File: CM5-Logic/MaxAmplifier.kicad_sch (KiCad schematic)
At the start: 8 parts, among them U12 MAX98357AETE_T, U13 MAX98357AETE_T

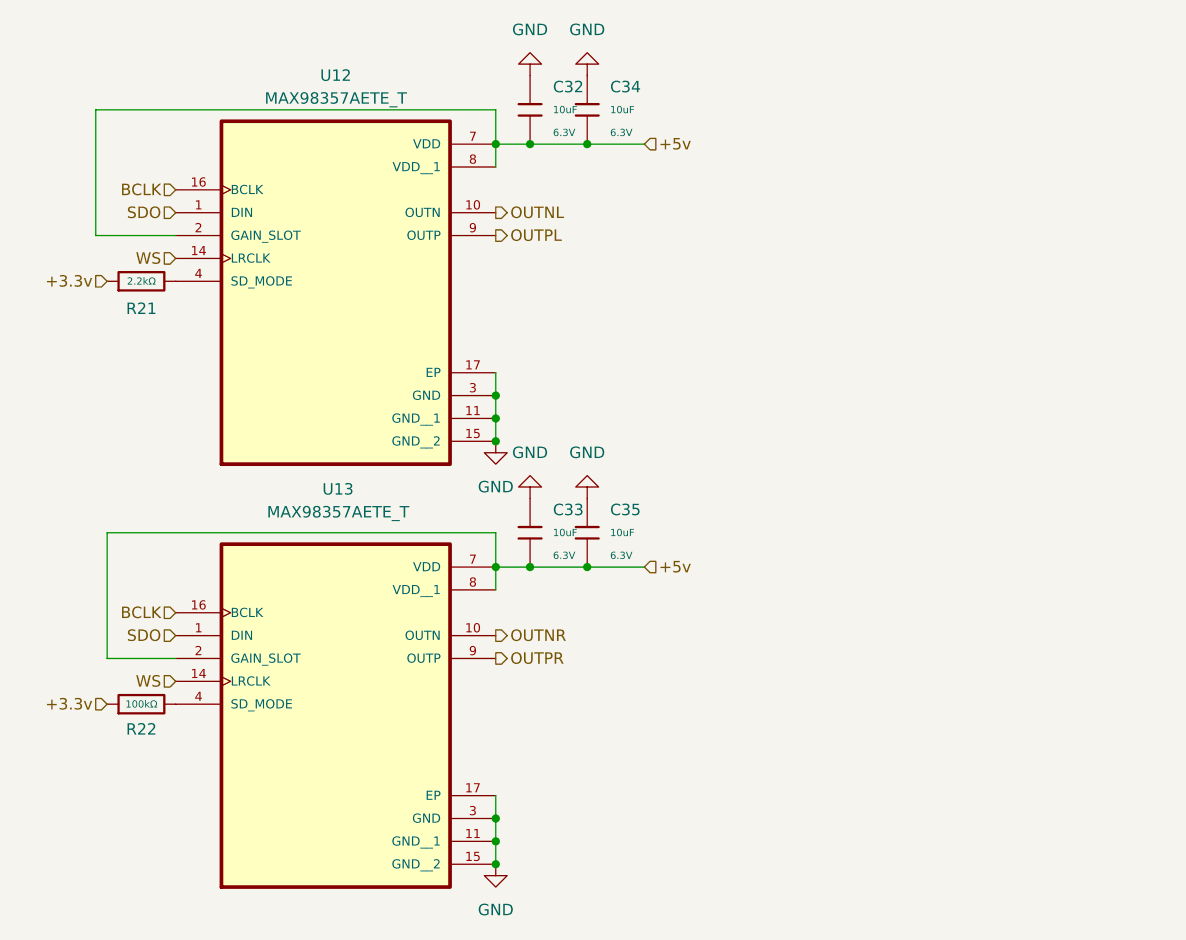
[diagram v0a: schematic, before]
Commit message: adds respeaker and reworks the amplifier
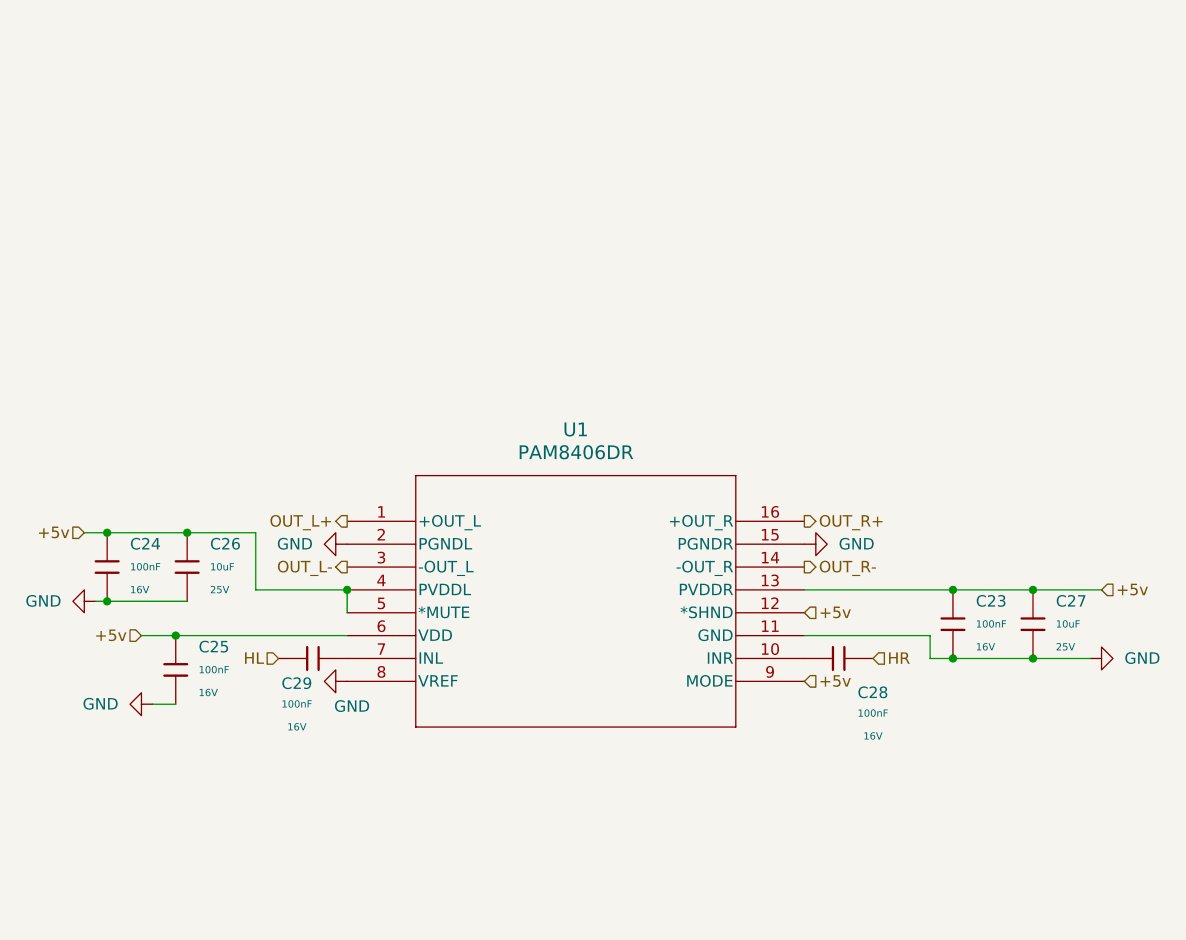
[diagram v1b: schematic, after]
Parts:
- removed C32, C33, C34, C35: 10uF, PCM_JLCPCB:C_0402, symbol PCM_JLCPCB-Capacitors:0402,10uF
- removed R21: 2.2kΩ, PCM_JLCPCB:R_0402, symbol PCM_JLCPCB-Resistors:0402,2.2kΩ
- removed R22: 100kΩ, PCM_JLCPCB:R_0402, symbol PCM_JLCPCB-Resistors:0402,100kΩ
- removed U12, U13: MAX98357AETE_T, Custom Components:QFN50P300X300X80-17N, symbol MAX98357AETE_T:MAX98357AETE_T
- added C23, C24, C25, C28, C29: 100nF, PCM_JLCPCB:C_0402, symbol PCM_JLCPCB-Capacitors:0402,100nF
- added C26, C27: 10uF, PCM_JLCPCB:C_0805, symbol PCM_JLCPCB-Capacitors:0805,10uF
- added U1: PAM8406DR, Custom Components:SO-16_PAM8406_DIO, symbol PAM8406_DIO:PAM8406DR
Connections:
- net +5v: now also C23.1, C24.1, C25.1, C26.1, C27.1, U1.12 (*SHND), U1.13 (PVDDR), U1.4 (PVDDL), U1.5 (*MUTE), U1.6 (VDD), U1.9 (MODE)
- net GND: now also C23.2, C24.2, C25.2, C26.2, C27.2, U1.11 (GND), U1.15 (PGNDR), U1.2 (PGNDL), U1.8 (VREF)
- new net: C28.2, U1.10 (INR)
- new net: C29.1, U1.7 (INL)
- new net HL: C29.2
- new net HR: C28.1
- new net OUT_L+: U1.1 (+OUT_L)
- new net OUT_L-: U1.3 (-OUT_L)
- new net OUT_R+: U1.16 (+OUT_R)
- new net OUT_R-: U1.14 (-OUT_R)
